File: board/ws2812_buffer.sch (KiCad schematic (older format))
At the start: 8 parts

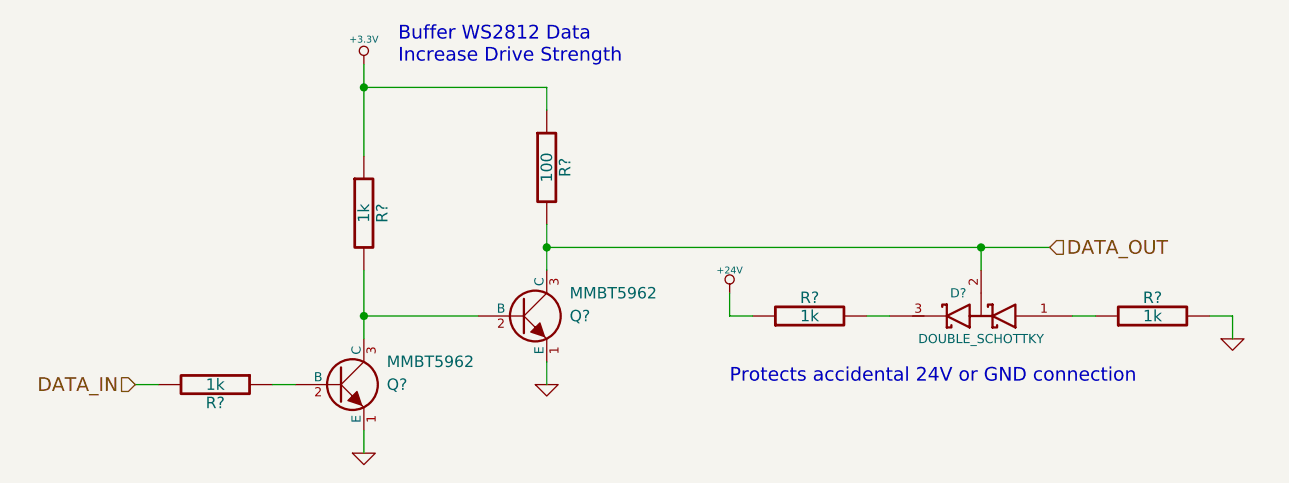
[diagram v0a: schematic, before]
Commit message: Removed double schottky
The double schottky wouldn't do much in this case. I have removed it.
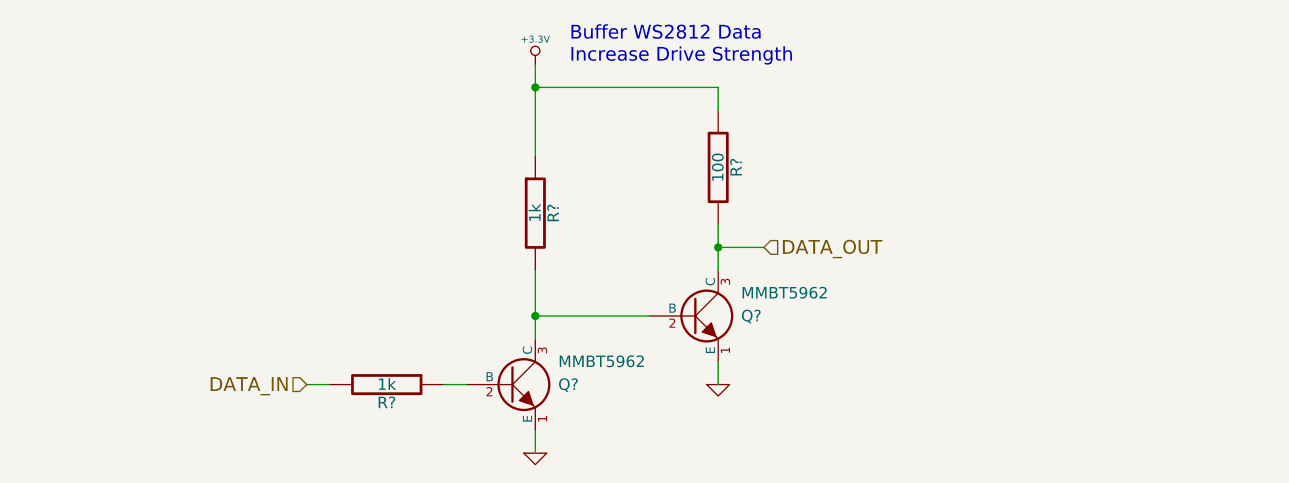
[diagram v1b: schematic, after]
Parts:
- removed D?: DOUBLE_SCHOTTKY, symbol DOUBLE_SCHOTTKY
- removed R? (x2): 1k, symbol R
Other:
- note removed: "Protects accidental 24V or GND connection"
- moved on the sheet: Q?, R?
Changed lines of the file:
@@
 L NPN Q?
 U 1 1 52EEEE15
-P 4500 4950
-F 0 "Q?" H 4700 4950 50  0000 L CNN
-F 1 "MMBT5962" H 4700 5050 50  0000 L CNN
-F 2 "" H 4500 4950 60  0000 C CNN
-F 3 "" H 4500 4950 60  0000 C CNN
-	1    4500 4950
+P 5250 4950
+F 0 "Q?" H 5450 4950 50  0000 L CNN
+F 1 "MMBT5962" H 5450 5050 50  0000 L CNN
+F 2 "" H 5250 4950 60  0000 C CNN
+F 3 "" H 5250 4950 60  0000 C CNN
+	1    5250 4950
 	1    0    0    -1
 $EndComp
@@
 L R R?
 U 1 1 52EEEE2E
-P 3950 4950
-F 0 "R?" V 4030 4950 50  0000 C CNN
-F 1 "1k" V 3950 4950 50  0000 C CNN
-F 2 "" H 3950 4950 60  0000 C CNN
-F 3 "" H 3950 4950 60  0000 C CNN
-	1    3950 4950
+P 4700 4950
+F 0 "R?" V 4780 4950 50  0000 C CNN
+F 1 "1k" V 4700 4950 50  0000 C CNN
+F 2 "" H 4700 4950 60  0000 C CNN
+F 3 "" H 4700 4950 60  0000 C CNN
+	1    4700 4950
 	0    1    1    0
 $EndComp
@@
 L GND #PWR?
 U 1 1 52EEEE49
-P 4600 5250
-F 0 "#PWR?" H 4600 5250 30  0001 C CNN
-F 1 "GND" H 4600 5180 30  0001 C CNN
-F 2 "" H 4600 5250 60  0000 C CNN
-F 3 "" H 4600 5250 60  0000 C CNN
-	1    4600 5250
+P 5350 5250
+F 0 "#PWR?" H 5350 5250 30  0001 C CNN
+F 1 "GND" H 5350 5180 30  0001 C CNN
+F 2 "" H 5350 5250 60  0000 C CNN
+F 3 "" H 5350 5250 60  0000 C CNN
+	1    5350 5250
 	1    0    0    -1
 $EndComp
@@
 L R R?
 U 1 1 52EEEE6D
-P 4600 4200
-F 0 "R?" V 4680 4200 50  0000 C CNN
-F 1 "1k" V 4600 4200 50  0000 C CNN
-F 2 "" H 4600 4200 60  0000 C CNN
-F 3 "" H 4600 4200 60  0000 C CNN
-	1    4600 4200
+P 5350 4200
+F 0 "R?" V 5430 4200 50  0000 C CNN
+F 1 "1k" V 5350 4200 50  0000 C CNN
+F 2 "" H 5350 4200 60  0000 C CNN
+F 3 "" H 5350 4200 60  0000 C CNN
+	1    5350 4200
 	1    0    0    -1
 $EndComp
@@
 L +3.3V #PWR?
 U 1 1 52EEEE7E
-P 4600 3550
-F 0 "#PWR?" H 4600 3510 30  0001 C CNN
-F 1 "+3.3V" H 4600 3660 30  0000 C CNN
-F 2 "" H 4600 3550 60  0000 C CNN
-F 3 "" H 4600 3550 60  0000 C CNN
-	1    4600 3550
+P 5350 3550
+F 0 "#PWR?" H 5350 3510 30  0001 C CNN
+F 1 "+3.3V" H 5350 3660 30  0000 C CNN
+F 2 "" H 5350 3550 60  0000 C CNN
+F 3 "" H 5350 3550 60  0000 C CNN
+	1    5350 3550
 	1    0    0    -1
 $EndComp
@@
 L NPN Q?
 U 1 1 52EEEE90
-P 5300 4650
-F 0 "Q?" H 5500 4650 50  0000 L CNN
-F 1 "MMBT5962" H 5500 4750 50  0000 L CNN
-F 2 "" H 5300 4650 60  0000 C CNN
-F 3 "" H 5300 4650 60  0000 C CNN
-	1    5300 4650
+P 6050 4650
+F 0 "Q?" H 6250 4650 50  0000 L CNN
+F 1 "MMBT5962" H 6250 4750 50  0000 L CNN
+F 2 "" H 6050 4650 60  0000 C CNN
+F 3 "" H 6050 4650 60  0000 C CNN
+	1    6050 4650
 	1    0    0    -1
 $EndComp
@@
 L GND #PWR?
 U 1 1 52EEEE97
-P 5400 4950
-F 0 "#PWR?" H 5400 4950 30  0001 C CNN
-F 1 "GND" H 5400 4880 30  0001 C CNN
-F 2 "" H 5400 4950 60  0000 C CNN
-F 3 "" H 5400 4950 60  0000 C CNN
-	1    5400 4950
+P 6150 4950
+F 0 "#PWR?" H 6150 4950 30  0001 C CNN
+F 1 "GND" H 6150 4880 30  0001 C CNN
+F 2 "" H 6150 4950 60  0000 C CNN
+F 3 "" H 6150 4950 60  0000 C CNN
+	1    6150 4950
 	1    0    0    -1
 $EndComp
@@
 L R R?
 U 1 1 52EEEE9E
-P 5400 4000
-F 0 "R?" V 5480 4000 50  0000 C CNN
-F 1 "100" V 5400 4000 50  0000 C CNN
-F 2 "" H 5400 4000 60  0000 C CNN
-F 3 "" H 5400 4000 60  0000 C CNN
-	1    5400 4000
+P 6150 4000
+F 0 "R?" V 6230 4000 50  0000 C CNN
+F 1 "100" V 6150 4000 50  0000 C CNN
+F 2 "" H 6150 4000 60  0000 C CNN
+F 3 "" H 6150 4000 60  0000 C CNN
+	1    6150 4000
 	1    0    0    -1
 $EndComp
-Text HLabel 3600 4950 0    60   Input ~ 0
+Text HLabel 4350 4950 0    60   Input ~ 0
 DATA_IN
-Text HLabel 7600 4350 2    60   Input ~ 0
+Text HLabel 6350 4350 2    60   Input ~ 0
 DATA_OUT
-$Comp
-L DOUBLE_SCHOTTKY D?
-U 1 1 52EECB3C
-P 7300 4650
-F 0 "D?" H 7400 4550 40  0000 C CNN
-F 1 "DOUBLE_SCHOTTKY" H 7300 4750 40  0000 C CNN
-F 2 "" H 7300 4650 60  0000 C CNN
-F 3 "" H 7300 4650 60  0000 C CNN
-	1    7300 4650
-	-1   0    0    1
-$EndComp
-$Comp
-L +24V #PWR?
-U 1 1 52EECBA2
-P 6200 4550
-F 0 "#PWR?" H 6200 4500 20  0001 C CNN
-F 1 "+24V" H 6200 4650 30  0000 C CNN
-F 2 "" H 6200 4550 60  0000 C CNN
-F 3 "" H 6200 4550 60  0000 C CNN
-	1    6200 4550
-	1    0    0    -1
-$EndComp
-$Comp
-L R R?
-U 1 1 52EECBC8
-P 8050 4650
-F 0 "R?" V 8130 4650 50  0000 C CNN
-F 1 "1k" V 8050 4650 50  0000 C CNN
-F 2 "" H 8050 4650 60  0000 C CNN
-F 3 "" H 8050 4650 60  0000 C CNN
-	1    8050 4650
-	0    -1   -1   0
-$EndComp
-$Comp
-L R R?
-U 1 1 52EECC02
-P 6550 4650
-F 0 "R?" V 6630 4650 50  0000 C CNN
-F 1 "1k" V 6550 4650 50  0000 C CNN
-F 2 "" H 6550 4650 60  0000 C CNN
-F 3 "" H 6550 4650 60  0000 C CNN
-	1    6550 4650
-	0    -1   -1   0
-$EndComp
-$Comp
-L GND #PWR?
-U 1 1 52EECC38
-P 8400 4750
-F 0 "#PWR?" H 8400 4750 30  0001 C CNN
-F 1 "GND" H 8400 4680 30  0001 C CNN
-F 2 "" H 8400 4750 60  0000 C CNN
-F 3 "" H 8400 4750 60  0000 C CNN
-	1    8400 4750
-	1    0    0    -1
-$EndComp
 Wire Wire Line
-	4200 4950 4300 4950
+	4950 4950 5050 4950
 Wire Wire Line
-	4600 5150 4600 5250
+	5350 5150 5350 5250
 Wire Wire Line
-	5400 4250 5400 4450
+	6150 4250 6150 4450
 Wire Wire Line
-	5400 3750 5400 3650
+	6150 3750 6150 3650
 Wire Wire Line
-	5400 4850 5400 4950
+	6150 4850 6150 4950
 Wire Wire Line
-	4600 4450 4600 4750
+	5350 4450 5350 4750
 Wire Wire Line
-	5100 4650 4600 4650
-Connection ~ 4600 4650
+	5850 4650 5350 4650
+Connection ~ 5350 4650
 Wire Wire Line
-	3600 4950 3700 4950
+	4350 4950 4450 4950
+Connection ~ 6150 4350
 Wire Wire Line
-	5400 4350 7600 4350
-Connection ~ 5400 4350
+	5350 3550 5350 3950
+Connection ~ 5350 3650
 Wire Wire Line
-	4600 3550 4600 3950
-Connection ~ 4600 3650
+	6150 3650 5350 3650
+Text Notes 5500 3550 0    60   ~ 0
+Buffer WS2812 Data\nIncrease Drive Strength
 Wire Wire Line
-	5400 3650 4600 3650
-Wire Wire Line
-	7300 4450 7300 4350
-Connection ~ 7300 4350
-Wire Wire Line
-	6300 4650 6200 4650
-Wire Wire Line
-	6200 4650 6200 4550
-Wire Wire Line
-	6900 4650 6800 4650
-Wire Wire Line
-	7700 4650 7800 4650
-Wire Wire Line
-	8300 4650 8400 4650
-Wire Wire Line
-	8400 4650 8400 4750
-Text Notes 4750 3550 0    60   ~ 0
-Buffer WS2812 Data\nIncrease Drive Strength
-Text Notes 6200 4950 0    60   ~ 0
-Protects accidental 24V or GND connection
+	6150 4350 6350 4350
 $EndSCHEMATC
